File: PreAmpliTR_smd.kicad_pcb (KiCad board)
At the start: 2 copper layers, 58.4 x 35.6 mm, 30 parts, among them J1 Conn_01x02, J2 Conn_01x02, J3 Conn_01x02, Q1 Q_NPN_BEC, Q2 Q_NPN_BEC

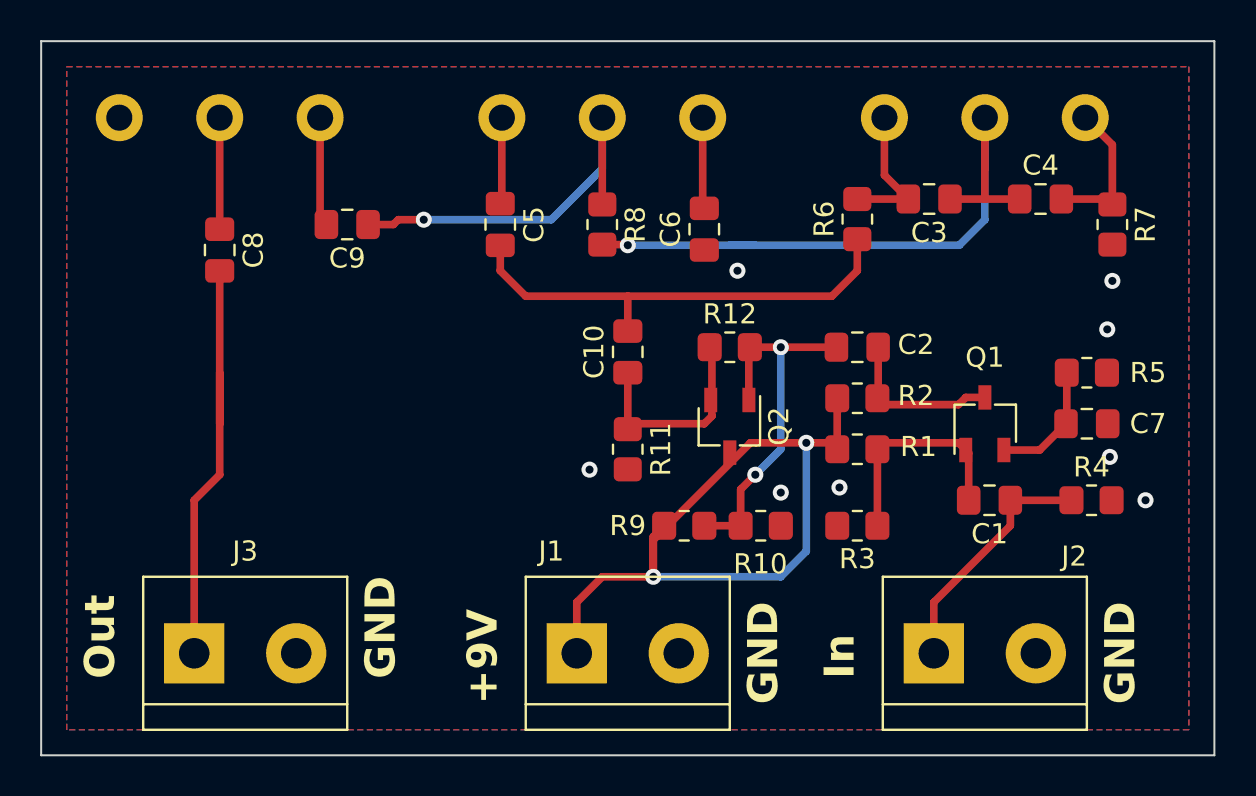
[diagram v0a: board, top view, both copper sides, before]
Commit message: cambio de bloques: ec - filtro - cc - salida
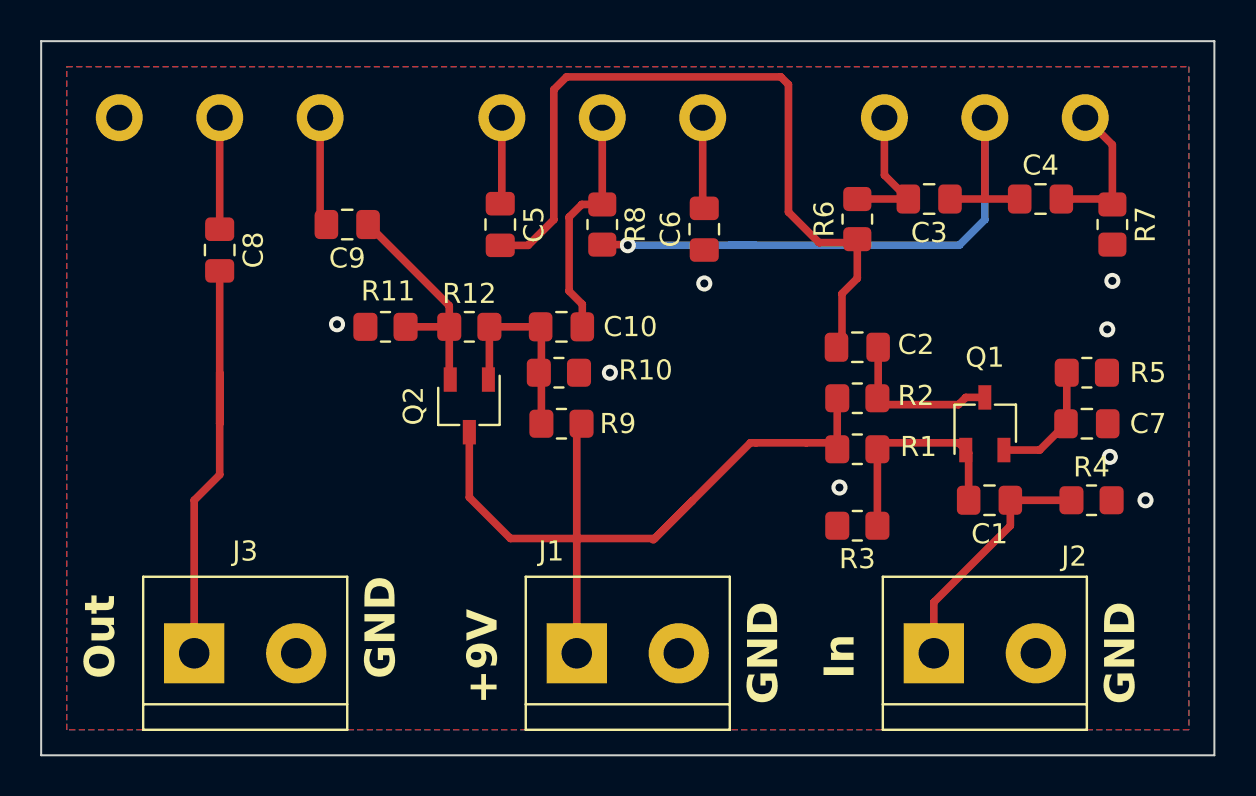
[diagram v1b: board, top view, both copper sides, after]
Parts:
- C3: value 100n -> 680p
- C4: value 100n -> 4700p
- C5: value 1n -> 470p
- C6: value 1n -> 4700p
- R6: value 3K3 -> 100k
- R7: value 3K3 -> 68k
- R8: value 6K8 -> 100k
- RV2, RV3: value 100K -> 1M
- moved R11 13.5 mm to (47.6, 91.7), turned to 180 degrees
- moved Q2 13.0 mm to (51.8, 95.6)
- moved R12 13.0 mm to (51.8, 91.7)
- moved R10 12.6 mm to (56.3, 94.0)
- moved R9 7.95 mm to (56.4, 96.5), turned to 180 degrees
- moved C10 3.53 mm to (56.4, 91.7), turned to 180 degrees
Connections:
- C10 pad 1: /CC_Out -> Net-(C10-Pad1)
- C10 pad 2: Net-(C10-Pad2) -> Net-(Q2-B)
- C2 pad 2: Net-(Q2-B) -> Net-(C2-Pad2)
- C5 pad 2: Net-(C10-Pad2) -> Net-(C2-Pad2)
- C9 pad 1: Net-(C9-Pad1) -> /CC_Out
- R6 pad 1: Net-(C10-Pad2) -> Net-(C2-Pad2)
- R8 pad 1: Net-(C9-Pad1) -> Net-(C10-Pad1)
- RV3 pad 2: Net-(C9-Pad1) -> Net-(C10-Pad1)
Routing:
- net Net-(C2-Pad2): track 0.00 -> 38.3 mm
- net Net-(C10-Pad2): track 23.6 -> 0.00 mm
- net Net-(C9-Pad1): track 20.0 -> 0.00 mm, vias 1 -> 0
- net Net-(C10-Pad1): track 0.00 -> 12.3 mm
- net Net-(Q2-B): track 18.4 -> 10.0 mm, vias 2 -> 0
- net +9V: track 38.9 -> 41.3 mm, vias 2 -> 0
